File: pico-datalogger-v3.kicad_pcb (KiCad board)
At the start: 2 copper layers, 130 x 65 mm, 59 parts, among them IC1 LM66200DRLR, J1 JST-PH2 Bat, J11 Conn_I2C1, J12 Conn_UART_5V, J13 THT_I2C1, J14 THT_I2C0, J17 Disp_THT, J2 Conn_Pico_Left, J3 Conn_Pico_Right, J4 SM06B-GHS-TB_LF_SN, J6 Conn_Display, J9 Conn_I2C0, Q1 AO3401A, Q2 AO3401A, SW1 SW_Push, SW2 SW_Push, SW3 SW_Push, SW4 SW_Push, SW5 SW_Push, U1 74LVC2G74, U2 PCF8523T, U4 XTSD, U5 SCD40_Breakout, U6 AHT20, U7 RFM95W-868S2, Y1 Crystal

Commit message: switch to user:SW_PUSH
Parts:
- SW1, SW2, SW3, SW4, SW5: footprint Button_Switch_SMD:SW_SPST_B3S-1000 -> user:SW_SPST_B3S-1000
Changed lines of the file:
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@@
     )
   )
-  (footprint "Button_Switch_SMD:SW_SPST_B3S-1000" (layer "B.Cu")
+  (footprint "user:SW_SPST_B3S-1000" (layer "B.Cu")
     (at 133.3 131.575 -90)
     (descr "Surface Mount Tactile Switch for High-Density Packaging")
@@
     (pad "2" smd rect (at 3.975 -2.25 270) (size 1.55 1.3) (layers "B.Cu" "B.Paste" "B.Mask")
       (net 2 "GND") (pinfunction "2") (pintype "passive"))
-    (model "${KICAD6_3DMODEL_DIR}/Button_Switch_SMD.3dshapes/SW_SPST_B3S-1000.wrl"
-      (offset (xyz 0 0 0))
-      (scale (xyz 1 1 1))
-      (rotate (xyz 0 0 0))
+    (model "/home/bablokb/kicad7/3dmodules/user.3dshapes/SPST-Button.step"
+      (offset (xyz 0 0 0))
+      (scale (xyz 1 1 1))
+      (rotate (xyz -90 0 0))
     )
   )
@@
     )
   )
-  (footprint "Button_Switch_SMD:SW_SPST_B3S-1000" (layer "B.Cu")
+  (footprint "user:SW_SPST_B3S-1000" (layer "B.Cu")
     (at 116.85 131.6 -90)
     (descr "Surface Mount Tactile Switch for High-Density Packaging")
@@
     (pad "2" smd rect (at 3.975 -2.25 270) (size 1.55 1.3) (layers "B.Cu" "B.Paste" "B.Mask")
       (net 2 "GND") (pinfunction "2") (pintype "passive"))
-    (model "${KICAD6_3DMODEL_DIR}/Button_Switch_SMD.3dshapes/SW_SPST_B3S-1000.wrl"
-      (offset (xyz 0 0 0))
-      (scale (xyz 1 1 1))
-      (rotate (xyz 0 0 0))
+    (model "/home/bablokb/kicad7/3dmodules/user.3dshapes/SPST-Button.step"
+      (offset (xyz 0 0 0))
+      (scale (xyz 1 1 1))
+      (rotate (xyz -90 0 0))
     )
   )
@@
     )
   )
-  (footprint "Button_Switch_SMD:SW_SPST_B3S-1000" (layer "B.Cu")
+  (footprint "user:SW_SPST_B3S-1000" (layer "B.Cu")
     (at 154.2 158.75 -90)
     (descr "Surface Mount Tactile Switch for High-Density Packaging")
@@
     (pad "2" smd rect (at 3.975 -2.25 270) (size 1.55 1.3) (layers "B.Cu" "B.Paste" "B.Mask")
       (net 2 "GND") (pinfunction "2") (pintype "passive"))
-    (model "${KICAD6_3DMODEL_DIR}/Button_Switch_SMD.3dshapes/SW_SPST_B3S-1000.wrl"
-      (offset (xyz 0 0 0))
-      (scale (xyz 1 1 1))
-      (rotate (xyz 0 0 0))
+    (model "/home/bablokb/kicad7/3dmodules/user.3dshapes/SPST-Button.step"
+      (offset (xyz 0 0 0))
+      (scale (xyz 1 1 1))
+      (rotate (xyz -90 0 0))
     )
   )
@@
       (net 6 "SDA") (pinfunction "SDA") (pintype "bidirectional"))
   )
-  (footprint "Button_Switch_SMD:SW_SPST_B3S-1000" (layer "B.Cu")
+  (footprint "user:SW_SPST_B3S-1000" (layer "B.Cu")
     (at 125 131.575 -90)
     (descr "Surface Mount Tactile Switch for High-Density Packaging")
@@
     (pad "2" smd rect (at 3.975 -2.25 270) (size 1.55 1.3) (layers "B.Cu" "B.Paste" "B.Mask")
       (net 2 "GND") (pinfunction "2") (pintype "passive"))
-    (model "${KICAD6_3DMODEL_DIR}/Button_Switch_SMD.3dshapes/SW_SPST_B3S-1000.wrl"
-      (offset (xyz 0 0 0))
-      (scale (xyz 1 1 1))
-      (rotate (xyz 0 0 0))
+    (model "/home/bablokb/kicad7/3dmodules/user.3dshapes/SPST-Button.step"
+      (offset (xyz 0 0 0))
+      (scale (xyz 1 1 1))
+      (rotate (xyz -90 0 0))
     )
   )
@@
       (net 48 "Net-(JP1-B)") (pinfunction "B") (pintype "passive"))
   )
-  (footprint "Button_Switch_SMD:SW_SPST_B3S-1000" (layer "B.Cu")
+  (footprint "user:SW_SPST_B3S-1000" (layer "B.Cu")
     (at 143.6 158.7 -90)
     (descr "Surface Mount Tactile Switch for High-Density Packaging")
@@
     (pad "2" smd rect (at 3.975 -2.25 270) (size 1.55 1.3) (layers "B.Cu" "B.Paste" "B.Mask")
       (net 2 "GND") (pinfunction "2") (pintype "passive"))
-    (model "${KICAD6_3DMODEL_DIR}/Button_Switch_SMD.3dshapes/SW_SPST_B3S-1000.wrl"
-      (offset (xyz 0 0 0))
-      (scale (xyz 1 1 1))
-      (rotate (xyz 0 0 0))
-    )
-  )
+    (model "/home/bablokb/kicad7/3dmodules/user.3dshapes/SPST-Button.step"
+      (offset (xyz 0 0 0))
+      (scale (xyz 1 1 1))
+      (rotate (xyz -90 0 0))
+    )
+  )

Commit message: switch to user:JST_SUR_BM08B-SURS-TF_1x08-1MP_P0.80mm_Vertical
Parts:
- J6: footprint Connector_JST:JST_SUR_BM08B-SURS-TF_1x08-1MP_P0.80mm_Vertical -> user:JST_SUR_BM08B-SURS-TF_1x08-1MP_P0.80mm_Vertical
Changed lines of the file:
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@@
     )
   )
-  (footprint "Connector_JST:JST_SUR_BM08B-SURS-TF_1x08-1MP_P0.80mm_Vertical" (layer "B.Cu")
+  (footprint "user:JST_SUR_BM08B-SURS-TF_1x08-1MP_P0.80mm_Vertical" (layer "B.Cu")
     (at 170.5 162.05 180)
     (descr "JST SUR series connector, BM08B-SURS-TF (http://www.jst-mfg.com/product/pdf/eng/eSUR.pdf), generated with kicad-footprint-generator")
@@
     (pad "8" smd roundrect (at 2.8 -0.85 180) (size 0.5 1.1) (layers "B.Cu" "B.Paste" "B.Mask") (roundrect_rratio 0.25)
       (net 8 "+3V3") (pinfunction "Pin_8") (pintype "passive"))
-    (pad "MP" smd roundrect (at -4.1 0.55 180) (size 1.2 1.7) (layers "B.Cu" "B.Paste" "B.Mask") (roundrect_rratio 0.2083333333))
-    (pad "MP" smd roundrect (at 4.1 0.55 180) (size 1.2 1.7) (layers "B.Cu" "B.Paste" "B.Mask") (roundrect_rratio 0.2083333333))
-    (model "${KICAD6_3DMODEL_DIR}/Connector_JST.3dshapes/JST_SUR_BM08B-SURS-TF_1x08-1MP_P0.80mm_Vertical.wrl"
-      (offset (xyz 0 0 0))
-      (scale (xyz 1 1 1))
-      (rotate (xyz 0 0 0))
+    (pad "MP" smd roundrect (at -4.1 0.55 180) (size 1.2 1.7) (layers "B.Cu" "B.Paste" "B.Mask") (roundrect_rratio 0.208333))
+    (pad "MP" smd roundrect (at 4.1 0.55 180) (size 1.2 1.7) (layers "B.Cu" "B.Paste" "B.Mask") (roundrect_rratio 0.208333))
+    (model "/home/bablokb/kicad7/3dmodules/user.3dshapes/JST_BM08B-SRSS-TB -LF-SN.step"
+      (offset (xyz 0 1.8 0))
+      (scale (xyz 0.8 1 1))
+      (rotate (xyz -90 0 0))
     )
   )
@@
     (property "ki_description" "Generic connector, single row, 01x08, script generated (kicad-library-utils/schlib/autogen/connector/)")
     (property "ki_keywords" "connector")
-    (attr through_hole exclude_from_pos_files exclude_from_bom)
-    (fp_text reference "J17" (at 0 2.33 90) (layer "B.SilkS") hide
-        (effects (font (size 1 1) (thickness 0.15)) (justify mirror))
-    )
-    (fp_text value "Disp_THT" (at 0 -20.11 90) (layer "B.Fab")
-        (effects (font (size 1 1) (thickness 0.15)) (justify mirror))
-    )
+    (attr through_hole exclude_from_bom)
+    (fp_text reference "J17" (at 0 2.33 270) (layer "B.SilkS") hide
+        (effects (font (size 1 1) (thickness 0.15)) (justify mirror))
+    )
+    (fp_text value "Disp_THT" (at 0 -20.11 270) (layer "B.Fab")
+        (effects (font (size 1 1) (thickness 0.15)) (justify mirror))
+    )

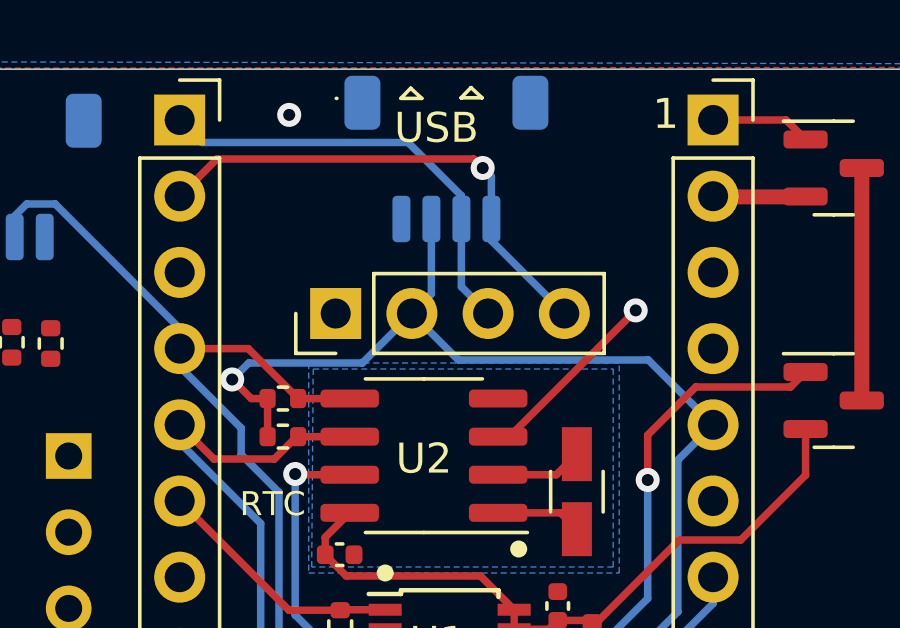
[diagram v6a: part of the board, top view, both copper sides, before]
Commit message: flipped I2C0-THT to back-side
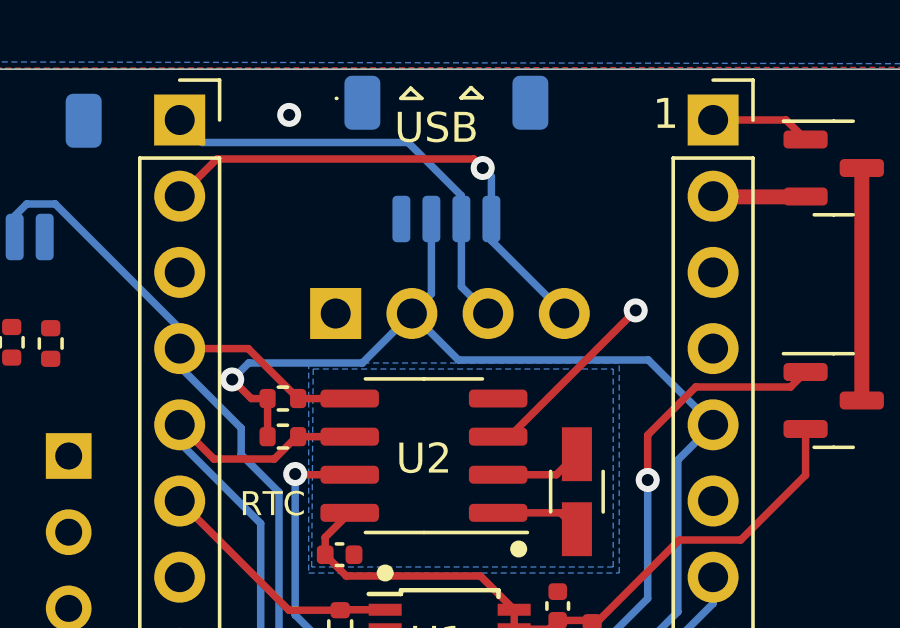
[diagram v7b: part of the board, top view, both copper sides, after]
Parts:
- J14: moved to B.Cu
- turned J14 to -90 degrees
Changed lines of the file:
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@@
     (pad "" np_thru_hole circle (at 0 0) (size 2.5 2.5) (drill 2.5) (layers "*.Cu" "*.Mask"))
-  )
-  (footprint "Connector_PinHeader_2.54mm:PinHeader_1x04_P2.54mm_Vertical" (layer "F.Cu")
-    (at 144.85 108.1 90)
-    (descr "Through hole straight pin header, 1x04, 2.54mm pitch, single row")
-    (tags "Through hole pin header THT 1x04 2.54mm single row")
-    (property "Sheetfile" "pico-datalogger-v3.kicad_sch")
-    (property "Sheetname" "")
-    (property "exclude_from_bom" "")
-    (property "ki_description" "Generic connector, single row, 01x04, script generated (kicad-library-utils/schlib/autogen/connector/)")
-    (property "ki_keywords" "connector")
-    (attr through_hole exclude_from_pos_files exclude_from_bom)
-    (fp_text reference "J14" (at 0 -2.33 90) (layer "F.SilkS") hide
-        (effects (font (size 1 1) (thickness 0.15)))
-    )
-    (fp_text value "THT_I2C0" (at 0 9.95 90) (layer "F.Fab") hide
-        (effects (font (size 1 1) (thickness 0.15)))
-    )
-    (fp_text user "${REFERENCE}" (at 0 3.81) (layer "F.Fab") hide
-        (effects (font (size 1 1) (thickness 0.15)))
-    )
-    (fp_line (start -1.33 -1.33) (end 0 -1.33)
-      (stroke (width 0.12) (type solid)) (layer "F.SilkS"))
-    (fp_line (start -1.33 0) (end -1.33 -1.33)
-      (stroke (width 0.12) (type solid)) (layer "F.SilkS"))
-    (fp_line (start -1.33 1.27) (end -1.33 8.95)
-      (stroke (width 0.12) (type solid)) (layer "F.SilkS"))
-    (fp_line (start -1.33 1.27) (end 1.33 1.27)
-      (stroke (width 0.12) (type solid)) (layer "F.SilkS"))
-    (fp_line (start -1.33 8.95) (end 1.33 8.95)
-      (stroke (width 0.12) (type solid)) (layer "F.SilkS"))
-    (fp_line (start 1.33 1.27) (end 1.33 8.95)
-      (stroke (width 0.12) (type solid)) (layer "F.SilkS"))
-    (fp_line (start -1.8 -1.8) (end -1.8 9.4)
-      (stroke (width 0.05) (type solid)) (layer "F.CrtYd"))
-    (fp_line (start -1.8 9.4) (end 1.8 9.4)
-      (stroke (width 0.05) (type solid)) (layer "F.CrtYd"))
-    (fp_line (start 1.8 -1.8) (end -1.8 -1.8)
-      (stroke (width 0.05) (type solid)) (layer "F.CrtYd"))
-    (fp_line (start 1.8 9.4) (end 1.8 -1.8)
-      (stroke (width 0.05) (type solid)) (layer "F.CrtYd"))
-    (fp_line (start -1.27 -0.635) (end -0.635 -1.27)
-      (stroke (width 0.1) (type solid)) (layer "F.Fab"))
-    (fp_line (start -1.27 8.89) (end -1.27 -0.635)
-      (stroke (width 0.1) (type solid)) (layer "F.Fab"))
-    (fp_line (start -0.635 -1.27) (end 1.27 -1.27)
-      (stroke (width 0.1) (type solid)) (layer "F.Fab"))
-    (fp_line (start 1.27 -1.27) (end 1.27 8.89)
-      (stroke (width 0.1) (type solid)) (layer "F.Fab"))
-    (fp_line (start 1.27 8.89) (end -1.27 8.89)
-      (stroke (width 0.1) (type solid)) (layer "F.Fab"))
-    (pad "1" thru_hole rect (at 0 0 90) (size 1.7 1.7) (drill 1) (layers "*.Cu" "*.Mask")
-      (net 2 "GND") (pinfunction "GND") (pintype "power_in"))
-    (pad "2" thru_hole oval (at 0 2.54 90) (size 1.7 1.7) (drill 1) (layers "*.Cu" "*.Mask")
-      (net 8 "+3V3") (pinfunction "Vcc") (pintype "power_in"))
-    (pad "3" thru_hole oval (at 0 5.08 90) (size 1.7 1.7) (drill 1) (layers "*.Cu" "*.Mask")
-      (net 11 "/TX") (pinfunction "SDA") (pintype "bidirectional"))
-    (pad "4" thru_hole oval (at 0 7.62 90) (size 1.7 1.7) (drill 1) (layers "*.Cu" "*.Mask")
-      (net 13 "/RX") (pinfunction "SCL") (pintype "bidirectional"))
-    (model "${KICAD6_3DMODEL_DIR}/Connector_PinHeader_2.54mm.3dshapes/PinHeader_1x04_P2.54mm_Vertical.wrl"
-      (offset (xyz 0 0 0))
-      (scale (xyz 1 1 1))
-      (rotate (xyz 0 0 0))
-    )
   )
   (footprint "MountingHole:MountingHole_2.5mm" (layer "F.Cu")
@@
     )
   )
+  (footprint "Connector_PinHeader_2.54mm:PinHeader_1x04_P2.54mm_Vertical" (layer "B.Cu")
+    (at 144.85 108.1 -90)
+    (descr "Through hole straight pin header, 1x04, 2.54mm pitch, single row")
+    (tags "Through hole pin header THT 1x04 2.54mm single row")
+    (property "Sheetfile" "pico-datalogger-v3.kicad_sch")
+    (property "Sheetname" "")
+    (property "exclude_from_bom" "")
+    (property "ki_description" "Generic connector, single row, 01x04, script generated (kicad-library-utils/schlib/autogen/connector/)")
+    (property "ki_keywords" "connector")
+    (attr through_hole exclude_from_pos_files exclude_from_bom)
+    (fp_text reference "J14" (at 0 2.33 90) (layer "B.SilkS") hide
+        (effects (font (size 1 1) (thickness 0.15)) (justify mirror))
+    )
+    (fp_text value "THT_I2C0" (at 0 -9.95 90) (layer "B.Fab") hide
+        (effects (font (size 1 1) (thickness 0.15)) (justify mirror))
+    )
+    (fp_text user "${REFERENCE}" (at 0 -3.81) (layer "B.Fab") hide
+        (effects (font (size 1 1) (thickness 0.15)) (justify mirror))
+    )
+    (fp_line (start -1.33 -8.95) (end 1.33 -8.95)
+      (stroke (width 0.12) (type solid)) (layer "B.SilkS"))
+    (fp_line (start -1.33 -1.27) (end -1.33 -8.95)
+      (stroke (width 0.12) (type solid)) (layer "B.SilkS"))
+    (fp_line (start -1.33 -1.27) (end 1.33 -1.27)
+      (stroke (width 0.12) (type solid)) (layer "B.SilkS"))
+    (fp_line (start -1.33 0) (end -1.33 1.33)
+      (stroke (width 0.12) (type solid)) (layer "B.SilkS"))
+    (fp_line (start -1.33 1.33) (end 0 1.33)
+      (stroke (width 0.12) (type solid)) (layer "B.SilkS"))
+    (fp_line (start 1.33 -1.27) (end 1.33 -8.95)
+      (stroke (width 0.12) (type solid)) (layer "B.SilkS"))
+    (fp_line (start -1.8 -9.4) (end 1.8 -9.4)
+      (stroke (width 0.05) (type solid)) (layer "B.CrtYd"))
+    (fp_line (start -1.8 1.8) (end -1.8 -9.4)
+      (stroke (width 0.05) (type solid)) (layer "B.CrtYd"))
+    (fp_line (start 1.8 -9.4) (end 1.8 1.8)
+      (stroke (width 0.05) (type solid)) (layer "B.CrtYd"))
+    (fp_line (start 1.8 1.8) (end -1.8 1.8)
+      (stroke (width 0.05) (type solid)) (layer "B.CrtYd"))
+    (fp_line (start -1.27 -8.89) (end -1.27 0.635)
+      (stroke (width 0.1) (type solid)) (layer "B.Fab"))
+    (fp_line (start -1.27 0.635) (end -0.635 1.27)
+      (stroke (width 0.1) (type solid)) (layer "B.Fab"))
+    (fp_line (start -0.635 1.27) (end 1.27 1.27)
+      (stroke (width 0.1) (type solid)) (layer "B.Fab"))
+    (fp_line (start 1.27 -8.89) (end -1.27 -8.89)
+      (stroke (width 0.1) (type solid)) (layer "B.Fab"))
+    (fp_line (start 1.27 1.27) (end 1.27 -8.89)
+      (stroke (width 0.1) (type solid)) (layer "B.Fab"))
+    (pad "1" thru_hole rect (at 0 0 270) (size 1.7 1.7) (drill 1) (layers "*.Cu" "*.Mask")
+      (net 2 "GND") (pinfunction "GND") (pintype "power_in"))
+    (pad "2" thru_hole oval (at 0 -2.54 270) (size 1.7 1.7) (drill 1) (layers "*.Cu" "*.Mask")
+      (net 8 "+3V3") (pinfunction "Vcc") (pintype "power_in"))
+    (pad "3" thru_hole oval (at 0 -5.08 270) (size 1.7 1.7) (drill 1) (layers "*.Cu" "*.Mask")
+      (net 11 "/TX") (pinfunction "SDA") (pintype "bidirectional"))
+    (pad "4" thru_hole oval (at 0 -7.62 270) (size 1.7 1.7) (drill 1) (layers "*.Cu" "*.Mask")
+      (net 13 "/RX") (pinfunction "SCL") (pintype "bidirectional"))
+    (model "${KICAD6_3DMODEL_DIR}/Connector_PinHeader_2.54mm.3dshapes/PinHeader_1x04_P2.54mm_Vertical.wrl"
+      (offset (xyz 0 0 0))
+      (scale (xyz 1 1 1))
+      (rotate (xyz 0 0 0))
+    )
+  )

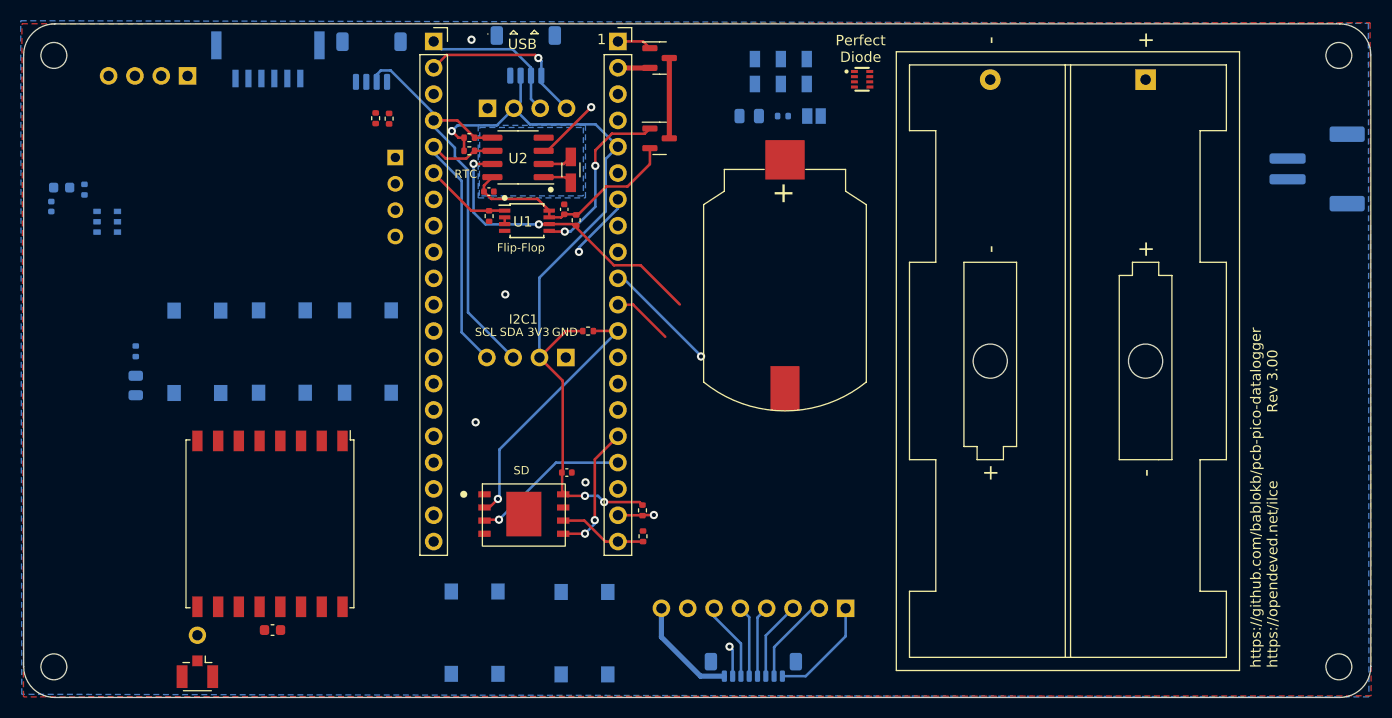
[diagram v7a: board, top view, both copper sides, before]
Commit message: improved silkscreen
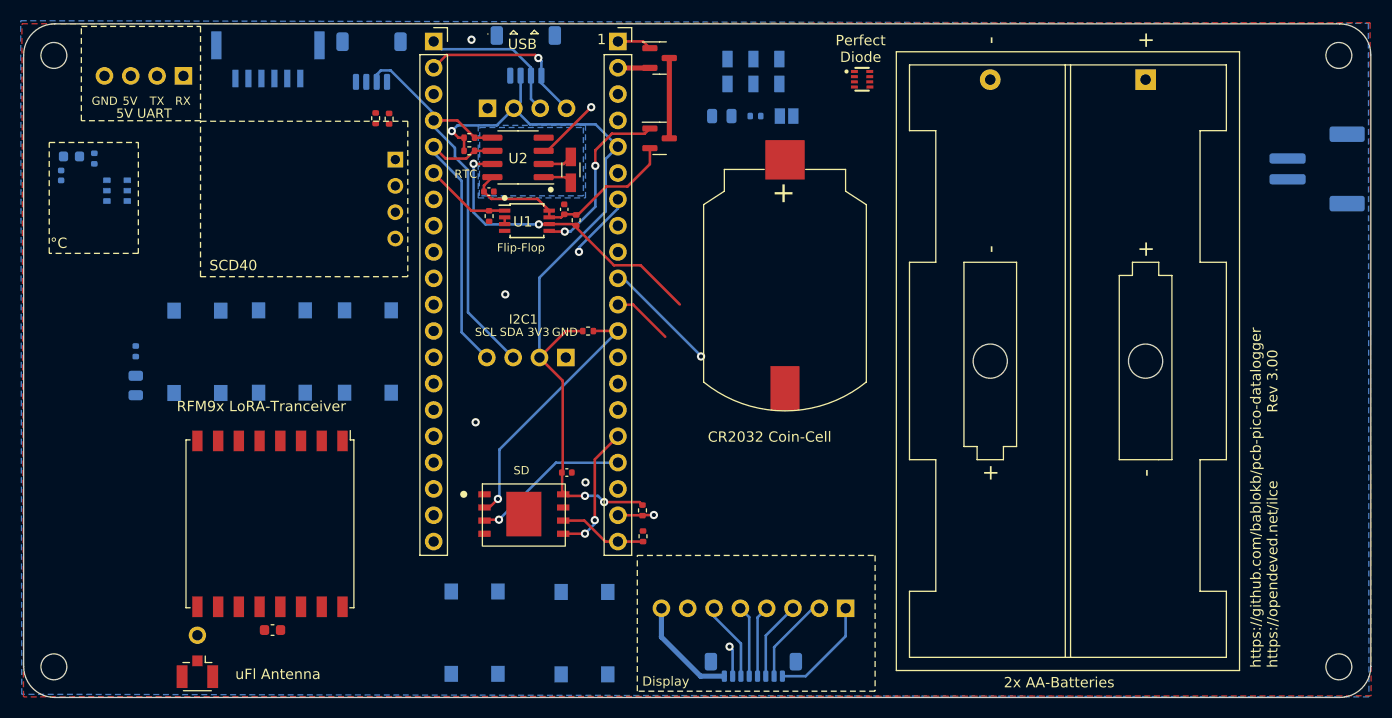
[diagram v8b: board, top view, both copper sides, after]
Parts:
- added G***: LOGO, user:giraffe, B.Cu at (199.4, 136.0)
- moved G*** 55.6 mm to (124.9, 151.6)
- moved C4 3.15 mm to (103.7, 114.6)
- moved C5 3.15 mm to (104.7, 112.8)
- moved R8 3.15 mm to (106.9, 113.0)
- moved U6 3.15 mm to (109.1, 116.0)
- moved S1 2.65 mm to (170.5, 104.5)
- moved D1 2.64 mm to (167.5, 108.8)
- moved JP1 2.64 mm to (173.7, 108.8)
- moved R11 2.64 mm to (170.7, 108.8)
- moved J12 0.40 mm to (115.5, 105.0)
- moved U5 0.20 mm to (135.9, 113.0)
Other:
- board text added: "2x AA-Batteries"
- board text added: "5V"
- board text added: "CR2032 Coin-Cell"
- board text added: "RFM9x LoRA-Tranceiver"
- board text added: "SCD40"
- board text added: "uFl Antenna"
